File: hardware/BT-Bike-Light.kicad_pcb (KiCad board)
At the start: 2 copper layers, 35 x 88.5 mm, 51 parts, among them J101 USB_C_Charge_Port, J102 SWD_Header, Q101 DMN3731U-7, Q601 DSG/CHG, SW101 Button, U101 BC805M, U102 TPS7A02, U201 MCP73834-xxx-MF, U301 STC3100IQT, U401 LIS2DTW12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

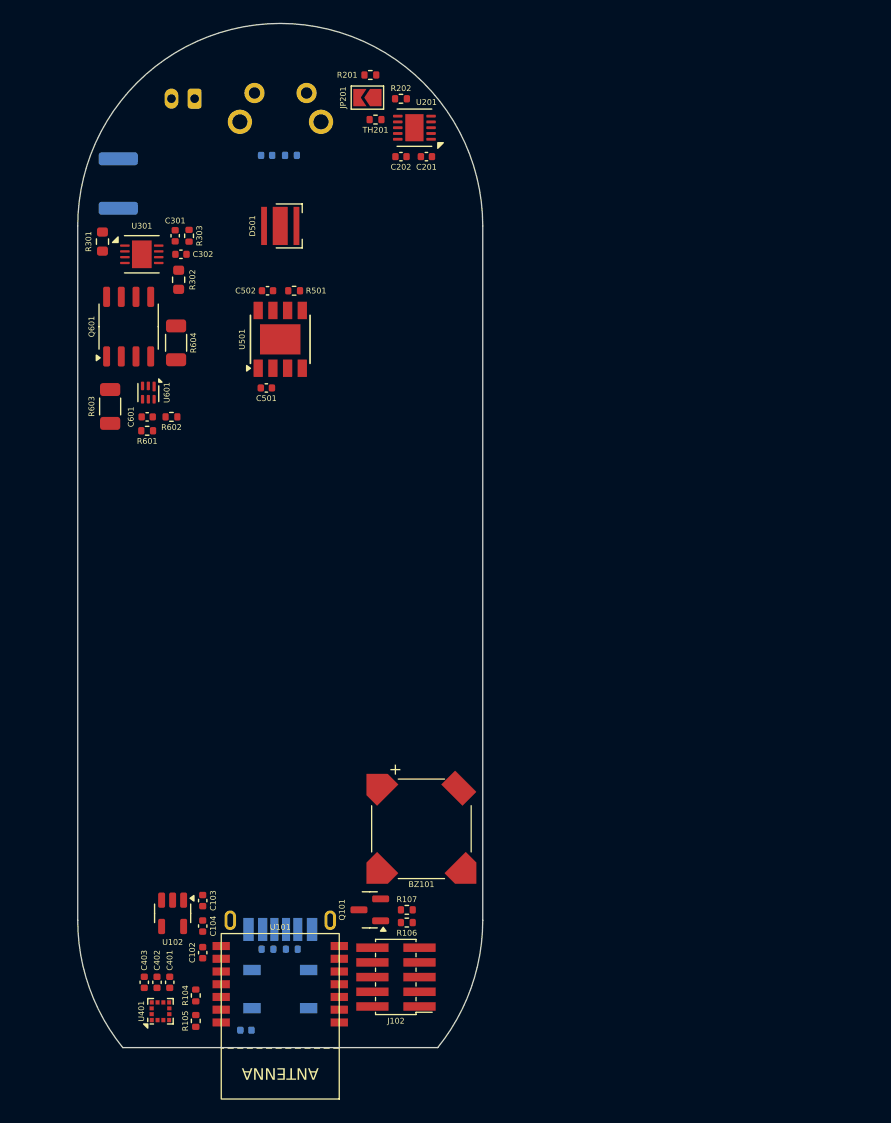
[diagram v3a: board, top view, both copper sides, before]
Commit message: Remove accelerometer, replace battery stuff with nPM1300
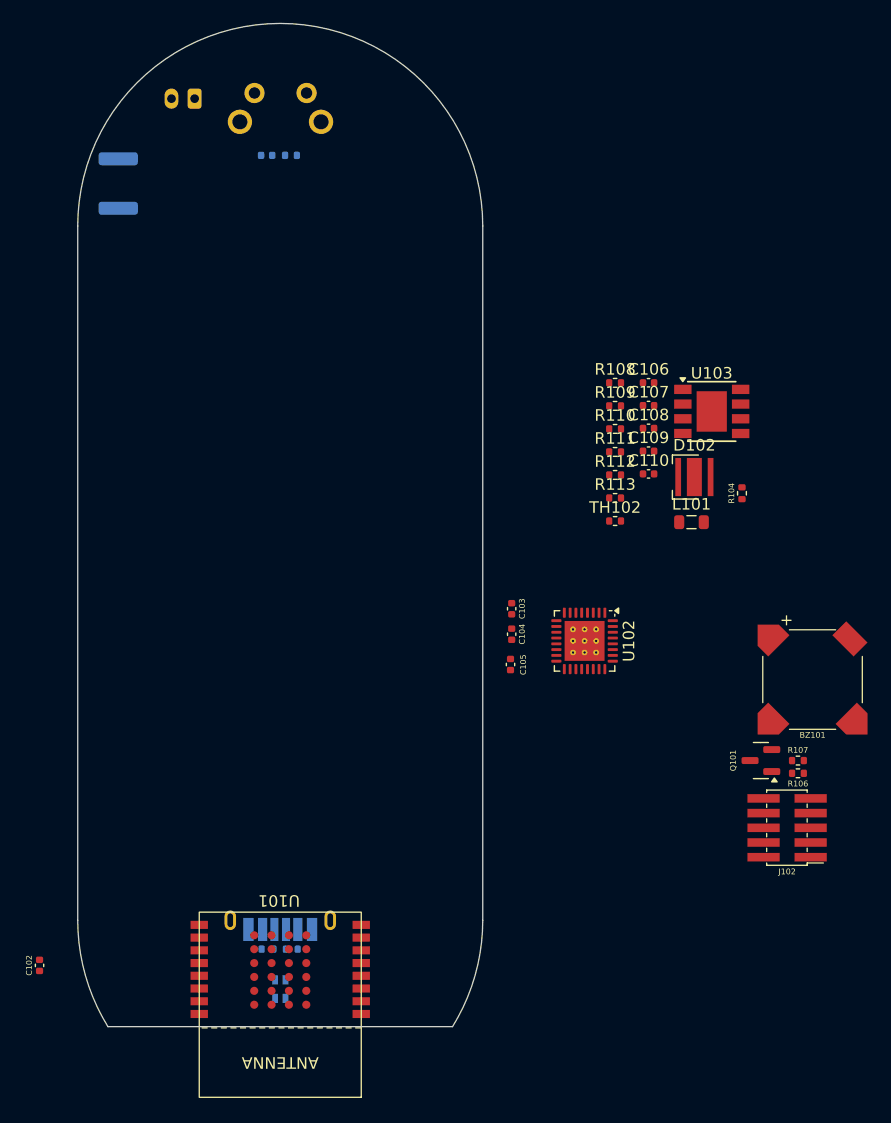
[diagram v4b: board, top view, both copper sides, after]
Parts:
- removed C201, C202, C302: 1uF, Capacitor_SMD:C_0402_1005Metric
- removed C301: 220nF, Capacitor_SMD:C_0402_1005Metric
- removed C401: 10uF, Capacitor_SMD:C_0402_1005Metric
- removed C402, C403, C601: 100nF, Capacitor_SMD:C_0402_1005Metric
- removed C501, C502: 4.7uF, Capacitor_SMD:C_0402_1005Metric
- removed D501: RED, LED_SMD:LED_Cree-XP
- removed JP201: TIM_DISABLE, Jumper:SolderJumper-2_P1.3mm_Open_TrianglePad1.0x1.5mm
- removed Q601: DSG/CHG, Package_SO:SO-8_3.9x4.9mm_P1.27mm
- removed R105, R201, TH201: 10K, Resistor_SMD:R_0402_1005Metric
- removed R202, R303: 1K, Resistor_SMD:R_0402_1005Metric
- removed R301: 200K, Resistor_SMD:R_0603_1608Metric
- removed R302: 0.03, Resistor_SMD:R_0603_1608Metric
- removed R501: 0.067, Resistor_SMD:R_0402_1005Metric
- removed R601: 330, Resistor_SMD:R_0402_1005Metric
- removed R602: 2.2K, Resistor_SMD:R_0402_1005Metric
- removed R603, R604: 5M, Resistor_SMD:R_1206_3216Metric
- removed U201: MCP73834-xxx-MF, Package_DFN_QFN:DFN-10-1EP_3x3mm_P0.5mm_EP1.58x2.35mm
- removed U301: STC3100IQT, Package_DFN_QFN:DFN-8-1EP_3x3mm_P0.5mm_EP1.7x2.4mm
- removed U401: LIS2DTW12, Package_LGA:LGA-12_2x2mm_P0.5mm
- removed U501: PAM2808, Package_SO:Diodes_SO-8EP
- removed U601: BQ297xy, Package_SON:WSON-6_1.5x1.5mm_P0.5mm
- added C106: 1uF, Capacitor_SMD:C_0402_1005Metric, F.Cu at (181.8, 85.2)
- added C107: 100nF, Capacitor_SMD:C_0402_1005Metric, F.Cu at (181.8, 87.2)
- added C108: 10uF, Capacitor_SMD:C_0402_1005Metric, F.Cu at (181.8, 89.2)
- added C109: 4.7uF, Capacitor_SMD:C_0402_1005Metric, F.Cu at (181.8, 91.2)
- added C110: 4.7uF, Capacitor_SMD:C_0402_1005Metric, F.Cu at (181.8, 93.1)
- added D102: RED, LED_SMD:LED_Cree-XP, F.Cu at (185.8, 93.4)
- added L101: 2.2uH, Inductor_SMD:L_0805_2012Metric, F.Cu at (185.5, 97.3)
- added R108: 110, Resistor_SMD:R_0402_1005Metric, F.Cu at (178.9, 85.3)
- added R109: 110, Resistor_SMD:R_0402_1005Metric, F.Cu at (178.9, 87.2)
- added R110: 10k, Resistor_SMD:R_0402_1005Metric, F.Cu at (178.9, 89.2)
- added R111: 110, Resistor_SMD:R_0402_1005Metric, F.Cu at (178.9, 91.2)
- added R112: 47k, Resistor_SMD:R_0402_1005Metric, F.Cu at (178.9, 93.2)
- added R113: 10k, Resistor_SMD:R_0402_1005Metric, F.Cu at (178.9, 95.2)
- added TH102: 10K, Resistor_SMD:R_0402_1005Metric, F.Cu at (178.9, 97.2)
- added U103: PAM2808, Package_SO:Diodes_SO-8EP, F.Cu at (187.3, 87.7)
- C104: value 1uF -> 10uF
- C105: value 100nF -> 10uF; moved to F.Cu
- D101: value WS2812B -> CHRG_LED; footprint LED_SMD:LED_WS2812B_PLCC4_5.0x5.0mm_P3.2mm -> Generic_Custom:LED_0606
- R104: value 10K -> 0.067
- U101: value BC805M -> BT832; footprint Fanstel:BC805M -> Fanstel:BT832
- U102: value TPS7A02 -> nPM1300; footprint Package_TO_SOT_SMD:SOT-23-5 -> Package_DFN_QFN:QFN-32-1EP_5x5mm_P0.5mm_EP3.45x3.45mm_ThermalVias
- moved R104 64.1 mm to (189.9, 94.8)
- moved U102 42.7 mm to (176.3, 107.6)
- moved C105 39.0 mm to (169.9, 109.6), turned to 90 degrees
- moved C103 36.7 mm to (170.0, 104.8)
- moved C104 36.7 mm to (170.0, 107.0)
- moved J102 36.2 mm to (195.8, 126.2)
- moved BZ101 36.2 mm to (196.0, 110.9)
- moved Q101 36.2 mm to (191.5, 117.9)
- moved R106 36.2 mm to (194.7, 119.0)
- moved R107 36.2 mm to (194.7, 117.9)
- moved C102 14.1 mm to (129.2, 135.6)
- moved U101 2.04 mm to (157.0, 139.8)
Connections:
- net /Battery Charger/BAT+ renamed Net-(BT101-+)
- BT101 pad 2: -BATT -> GND
- C103 pad 1: +BATT -> VBUS
- C104 pad 1: +1V8 -> VSYS
- C105 pad 1: +5V -> VSYS
- D101 pad 1: +5V -> Net-(D101-GK)
- D101 pad 2: unconnected-(D101-DOUT-Pad2) -> Net-(D101-BK)
- D101 pad 3: GND -> VSYS
- D101 pad 4: /LED_STAT -> Net-(D101-RK)
- F101 pad 2: +BATT -> Net-(U102-NTC)
- J101 pad A5: Net-(J101-CC1) -> /CC1
- J101 pad A9: +5V -> VBUS
- J101 pad B5: Net-(J101-CC2) -> /CC2
- J101 pad B9: +5V -> VBUS
- J102 pad 10: unconnected-(J102-~{RESET}-Pad10) -> /nRST
- R102 pad 2: Net-(J101-CC2) -> /CC2
- R103 pad 2: Net-(J101-CC1) -> /CC1
- R104 pad 1: +1V8 -> GND
- R104 pad 2: /SDA -> Net-(D102-K)
- U101 pad 1: /SWDIO -> unconnected-(U101-P026-Pad1)
- U101 pad 10: /LED_EN -> GND
- U101 pad 11: /BTN -> unconnected-(U101-P013-Pad11)
- U101 pad 12: /ACCEL_INT1 -> unconnected-(U101-P018-Pad12)
- U101 pad 13: /SDA -> unconnected-(U101-P020-Pad13)
- U101 pad 14: /SCL -> /nRST
- U101 pad 2: /SWCLK -> unconnected-(U101-P027-Pad2)
- U101 pad 3: /ACCEL_INT2 -> unconnected-(U101-P000-Pad3)
- U101 pad 4: /LED_STAT -> unconnected-(U101-P001-Pad4)
- U101 pad 5: /BUZZER -> unconnected-(U101-P002-Pad5)
- U101 pad 6: /CHRG_STAT2 -> unconnected-(U101-P003-Pad6)
- U101 pad 7: /CHRG_STAT1 -> unconnected-(U101-P009-Pad7)
- U101 pad 8: GND -> unconnected-(U101-P010-Pad8)
- U102 pad 1: +BATT -> +1V8
- U102 pad 3: +BATT -> Net-(U102-SW1)
- U102 pad 4: unconnected-(U102-NC-Pad4) -> VSYS
- U102 pad 5: +1V8 -> unconnected-(U102-SW2-Pad5)
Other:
- board size 35 x 88.5 mm -> 35 x 86.7 mm

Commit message: Place components
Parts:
- removed R102, R103: 5.1K, Resistor_SMD:R_0402_1005Metric
- added C111: 1uF, Capacitor_SMD:C_0402_1005Metric, F.Cu at (148.4, 117.2)
- D101, F101, J101: moved to F.Cu
- moved BT101 76.8 mm to (161.2, 135.2), turned to 0 degrees
- moved F101 58.2 mm to (150.4, 124.4), turned to 180 degrees
- moved J102 57.1 mm to (138.7, 128.1)
- moved C107 53.5 mm to (142.4, 123.4), turned to 90 degrees
- moved L101 51.6 mm to (137.9, 117.1), turned to 90 degrees
- moved C108 50.1 mm to (139.5, 116.0), turned to -90 degrees
- moved C106 48.8 mm to (148.4, 120.8)
- moved R110 48.3 mm to (144.8, 123.4), turned to -90 degrees
- moved R113 45.3 mm to (143.5, 123.4), turned to -90 degrees
- moved R112 44.3 mm to (146.5, 123.4), turned to 90 degrees
- moved R108 44.1 mm to (145.6, 114.1), turned to -90 degrees
- moved R104 43.8 mm to (151.9, 73.0), turned to 180 degrees
- moved D102 42.8 mm to (150.0, 70.0), turned to 180 degrees
- moved R109 42.0 mm to (146.7, 114.1), turned to -90 degrees
- moved R111 41.4 mm to (144.5, 114.1), turned to -90 degrees
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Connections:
- net /CC1 renamed Net-(J101-CC1)
- net /CC2 renamed Net-(J101-CC2)
- BZ101 pad 1: +BATT -> VBUSOUT
- C106 pad 1: +BATT -> Net-(U102-VBAT)
- C109 pad 1: +BATT -> VBUSOUT
- R107 pad 1: +BATT -> VBUSOUT
- U101 pad 11: unconnected-(U101-P013-Pad11) -> /SDA
- U101 pad 12: unconnected-(U101-P018-Pad12) -> /SCL
- U101 pad 13: unconnected-(U101-P020-Pad13) -> /BTN
- U101 pad 7: unconnected-(U101-P009-Pad7) -> /LED_EN
- U101 pad 8: unconnected-(U101-P010-Pad8) -> /BUZZER
- U102 pad 19: +BATT -> Net-(U102-VBAT)
- U102 pad 22: VBUS -> VBUSOUT
- U103 pad 2: +BATT -> VBUSOUT

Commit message: Schematic cleanup
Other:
- board text added: "REV.${REVISION} ${COMPANY} ${CURRENT_DATE}"
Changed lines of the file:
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@@
 	(title_block
 		(title "Bluetooth Bike Light")
-		(date "2024-08-24")
-		(rev "A")
+		(date "2024-08-30")
+		(rev "00A")
 		(company "Embedded Shark, LLC")
 		(comment 1 "Ben Owen")
@@
 		(layer "Edge.Cuts")
 	)
+	(gr_text "REV.${REVISION}\n${COMPANY}\n${CURRENT_DATE}"
+		(at 137.3 105 0)
+		(layer "F.SilkS" knockout)
+		(effects
+			(font
+				(size 1.5 1.5)
+				(thickness 0.3)
+				(bold yes)
+			)
+			(justify left)
+		)
+	)
 	(dimension
